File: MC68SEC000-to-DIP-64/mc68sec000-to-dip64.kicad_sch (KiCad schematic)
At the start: 5 parts, among them U2 68010D

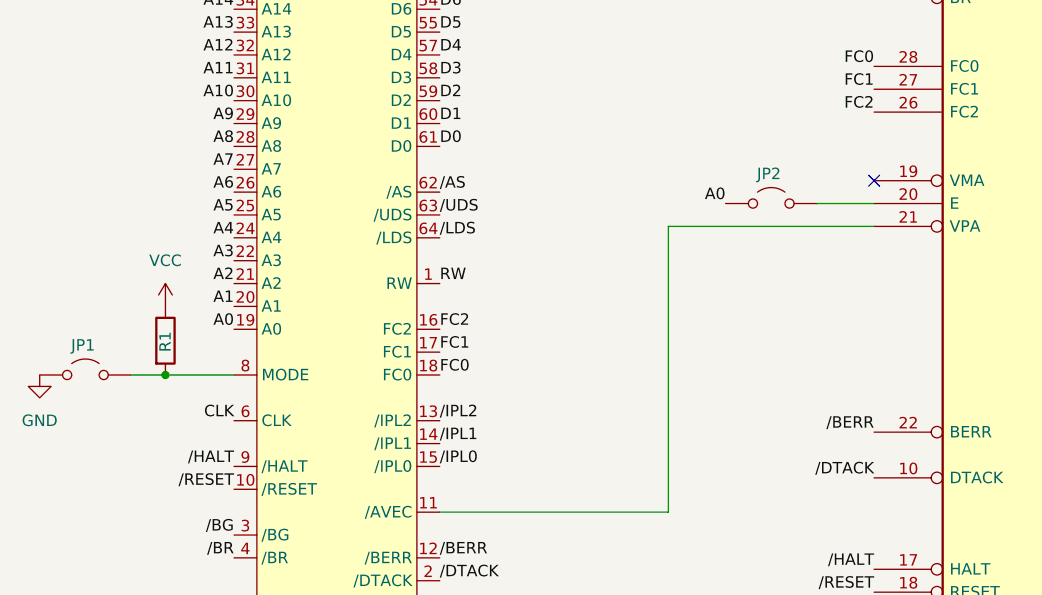
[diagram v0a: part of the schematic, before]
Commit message: Use larger footprint for MC68SEC000 QFP-64 IC
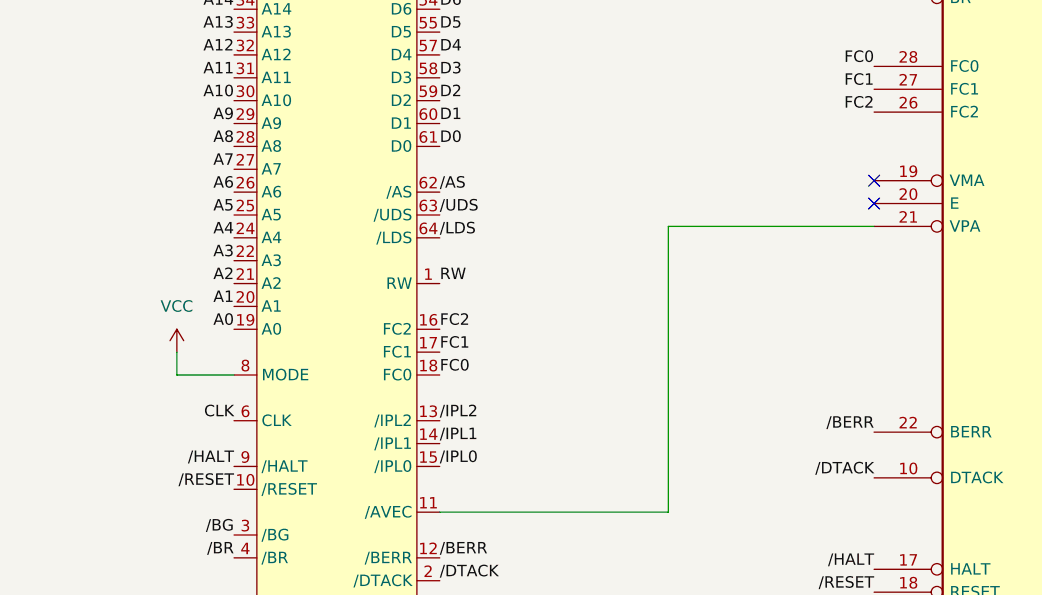
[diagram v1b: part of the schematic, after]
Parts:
- removed JP1, JP2: Jumper_2_Open, Connector_PinHeader_2.54mm:PinHeader_1x02_P2.54mm_Vertical, symbol Jumper:Jumper_2_Open
- removed R1: R, Resistor_SMD:R_1206_3216Metric_Pad1.30x1.75mm_HandSolder, symbol Device:R
- U1: footprint Package_QFP:LQFP-64_14x14mm_P0.8mm -> Package_QFP:PQFP-64_14x14mm_P0.8mm
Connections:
- net VCC: now also U1.8 (MODE)
- no-connect marks 2 -> 3
